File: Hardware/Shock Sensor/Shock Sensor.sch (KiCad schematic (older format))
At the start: 7 parts, among them J1 LED, J2 ACCEL, J3 RESET, SW2 ADDRESS, U1 WeMos_mini

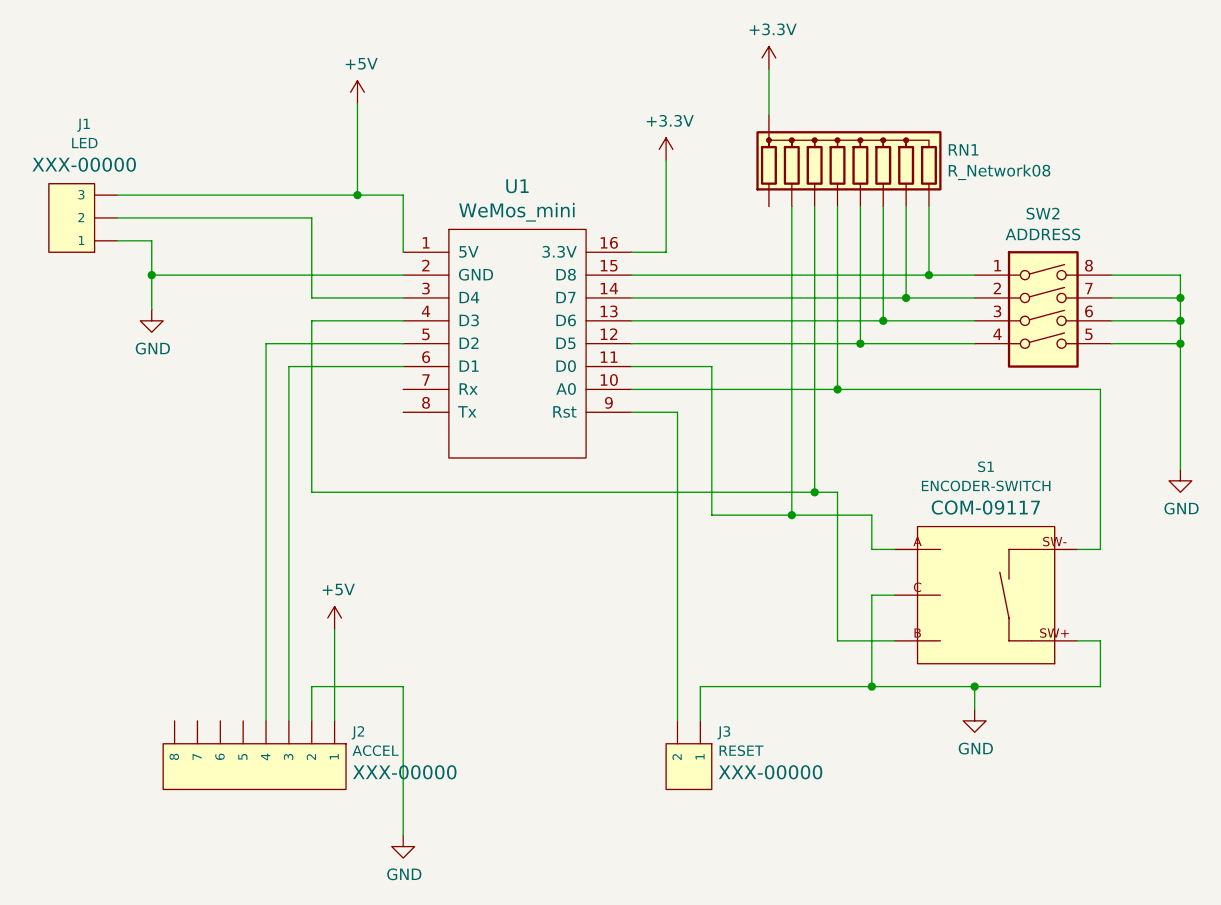
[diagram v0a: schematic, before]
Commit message: Updates to PCB and code for shock sensors
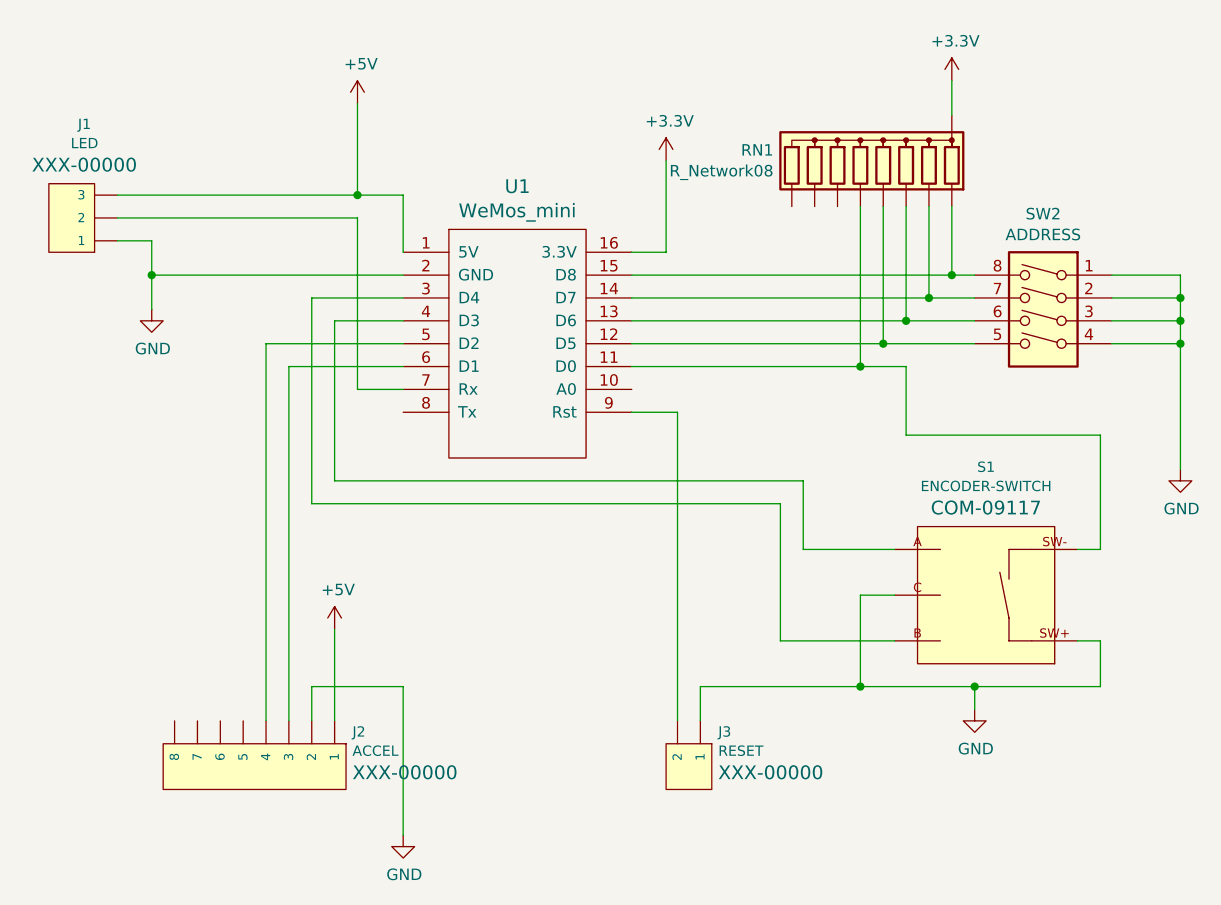
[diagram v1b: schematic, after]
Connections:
- net GND: now also SW2.1, SW2.2, SW2.3, SW2.4; no longer SW2.5, SW2.6, SW2.7, SW2.8
- net at U1.3 (D4): now also S1.B; no longer J1.2
- net at U1.7 (Rx): now also J1.2
- net at RN1.2 (R1): now also SW2.8, U1.15 (D8)
- new net: RN1.6 (R5), S1.SW-, U1.11 (D0)
- new net: RN1.5 (R4), SW2.5, U1.12 (D5)
- new net: RN1.4 (R3), SW2.6, U1.13 (D6)
- new net: RN1.3 (R2), SW2.7, U1.14 (D7)
- new net: S1.A, U1.4 (D3)
- now unconnected: RN1.7 (R6), RN1.8 (R7), RN1.9 (R8), U1.10 (A0)
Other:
- moved on the sheet: RN1
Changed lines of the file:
@@
 EESchema Schematic File Version 4
+LIBS:Shock Sensor-cache
 EELAYER 26 0
 EELAYER END
@@
 F 3 "" H 6950 3700 50  0001 C CNN
 	1    6950 3700
-	1    0    0    -1
+	-1   0    0    -1
 $EndComp
 $Comp
@@
 L power:+3.3V #PWR05
 U 1 1 5D7EFBA0
-P 5750 2600
-F 0 "#PWR05" H 5750 2450 50  0001 C CNN
-F 1 "+3.3V" H 5765 2773 50  0000 C CNN
-F 2 "" H 5750 2600 50  0001 C CNN
-F 3 "" H 5750 2600 50  0001 C CNN
-	1    5750 2600
+P 6550 2650
+F 0 "#PWR05" H 6550 2500 50  0001 C CNN
+F 1 "+3.3V" H 6565 2823 50  0000 C CNN
+F 2 "" H 6550 2650 50  0001 C CNN
+F 3 "" H 6550 2650 50  0001 C CNN
+	1    6550 2650
 	1    0    0    -1
 $EndComp
@@
 	6650 5300 6650 5400
 Connection ~ 6650 5300
-Wire Wire Line
-	6050 4450 6050 5100
-Wire Wire Line
-	3750 4450 3750 3700
-Wire Wire Line
-	3750 3700 4150 3700
 $Comp
 L Device:R_Network08 RN1
@@
 F 3 "http://www.vishay.com/docs/31509/csc.pdf" H 6150 3000 50  0001 C CNN
 	1    6150 3000
-	1    0    0    -1
-$EndComp
-Wire Wire Line
-	3750 4450 5950 4450
-Wire Wire Line
-	5150 4000 6050 4000
-Wire Wire Line
-	5150 3800 6150 3800
-Wire Wire Line
-	5150 3600 6350 3600
-Wire Wire Line
-	5150 3500 6450 3500
-Wire Wire Line
-	5750 2800 5750 2600
-Wire Wire Line
-	6450 3200 6450 3500
-Connection ~ 6450 3500
-Wire Wire Line
-	6450 3500 6650 3500
-Wire Wire Line
-	6350 3200 6350 3600
-Connection ~ 6350 3600
-Wire Wire Line
-	6350 3600 6650 3600
-Wire Wire Line
-	6250 3200 6250 3700
-Wire Wire Line
-	5150 3700 6250 3700
-Connection ~ 6250 3700
-Wire Wire Line
-	6250 3700 6650 3700
-Wire Wire Line
-	6150 3200 6150 3800
-Connection ~ 6150 3800
-Wire Wire Line
-	6150 3800 6650 3800
-Wire Wire Line
-	6050 3200 6050 4000
-Connection ~ 6050 4000
-Wire Wire Line
-	5950 3200 5950 4450
-Connection ~ 5950 4450
-Wire Wire Line
-	5950 4450 6050 4450
-Wire Wire Line
-	6200 4550 5850 4550
-Wire Wire Line
-	5500 4550 5500 3900
-Wire Wire Line
-	5500 3900 5150 3900
-Wire Wire Line
-	5850 3200 5850 4550
-Connection ~ 5850 4550
-Wire Wire Line
-	5850 4550 5500 4550
-Wire Wire Line
-	4150 3600 3750 3600
-Wire Wire Line
-	3750 3600 3750 3250
-Wire Wire Line
-	3750 3250 2900 3250
+	-1   0    0    -1
+$EndComp
 $Comp
 L power:GND #PWR01
@@
 $EndComp
 Wire Wire Line
-	7200 4000 7200 4700
-Wire Wire Line
 	7200 4700 7100 4700
 Wire Wire Line
-	6050 4000 7200 4000
-Wire Wire Line
 	7200 5300 7200 5100
 Wire Wire Line
@@
 Wire Wire Line
 	6650 5300 7200 5300
-Wire Wire Line
-	5450 5300 6200 5300
-Wire Wire Line
-	6300 5100 6050 5100
-Wire Wire Line
-	6300 4700 6200 4700
-Wire Wire Line
-	6200 4700 6200 4550
-Wire Wire Line
-	6300 4900 6200 4900
-Wire Wire Line
-	6200 4900 6200 5300
-Connection ~ 6200 5300
-Wire Wire Line
-	6200 5300 6650 5300
 $Comp
 L power:+3.3V #PWR0101
@@
 Wire Wire Line
 	5300 3400 5300 3000
+Wire Wire Line
+	3950 3250 3950 4000
+Wire Wire Line
+	3950 4000 4150 4000
+Wire Wire Line
+	2900 3250 3950 3250
+Wire Wire Line
+	6550 2650 6550 2800
+Wire Wire Line
+	5450 5300 6150 5300
+Wire Wire Line
+	6350 3900 6350 4200
+Wire Wire Line
+	6350 4200 7200 4200
+Wire Wire Line
+	7200 4200 7200 4700
+Wire Wire Line
+	6300 4900 6150 4900
+Wire Wire Line
+	6150 4900 6150 5300
+Connection ~ 6150 5300
+Wire Wire Line
+	6150 5300 6650 5300
+Wire Wire Line
+	4150 3600 3750 3600
+Wire Wire Line
+	4150 3700 3850 3700
+Wire Wire Line
+	3850 3700 3850 4400
+Wire Wire Line
+	3850 4400 5900 4400
+Wire Wire Line
+	5900 4400 5900 4700
+Wire Wire Line
+	5900 4700 6300 4700
+Wire Wire Line
+	3750 4500 5800 4500
+Wire Wire Line
+	5800 4500 5800 5100
+Wire Wire Line
+	5800 5100 6300 5100
+Wire Wire Line
+	3750 3600 3750 4500
+Wire Wire Line
+	5150 3500 6550 3500
+Wire Wire Line
+	5150 3600 6450 3600
+Wire Wire Line
+	5150 3700 6350 3700
+Wire Wire Line
+	5150 3800 6250 3800
+Wire Wire Line
+	5150 3900 6150 3900
+Wire Wire Line
+	6550 3200 6550 3500
+Connection ~ 6550 3500
+Wire Wire Line
+	6550 3500 6650 3500
+Wire Wire Line
+	6450 3200 6450 3600
+Connection ~ 6450 3600
+Wire Wire Line
+	6450 3600 6650 3600
+Wire Wire Line
+	6350 3200 6350 3700
+Connection ~ 6350 3700
+Wire Wire Line
+	6350 3700 6650 3700
+Wire Wire Line
+	6250 3200 6250 3800
+Connection ~ 6250 3800
+Wire Wire Line
+	6250 3800 6650 3800
+Wire Wire Line
+	6150 3200 6150 3900
+Connection ~ 6150 3900
+Wire Wire Line
+	6150 3900 6350 3900
 $EndSCHEMATC
